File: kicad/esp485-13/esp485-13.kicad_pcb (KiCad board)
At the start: 2 copper layers, 22.2 x 20.3 mm, 16 parts, among them J1 Conn_01x08, U1 MAX3485, U2 ESP-WROOM-02, U3 AMS1117-3.3

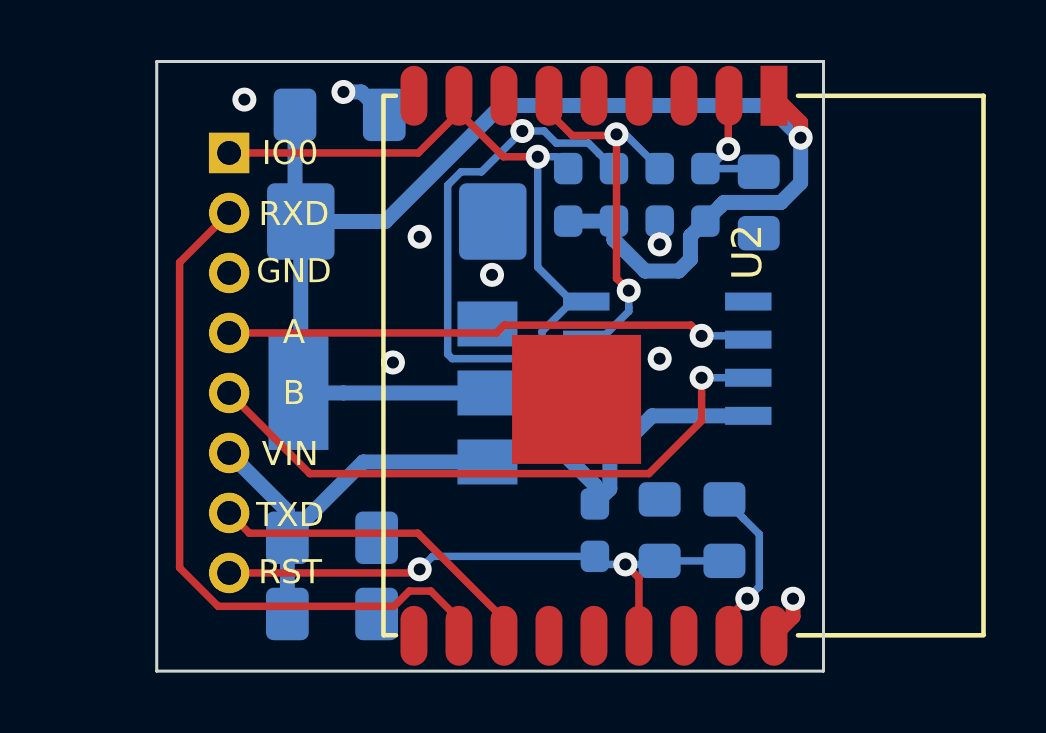
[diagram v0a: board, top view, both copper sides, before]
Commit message: arrange silks
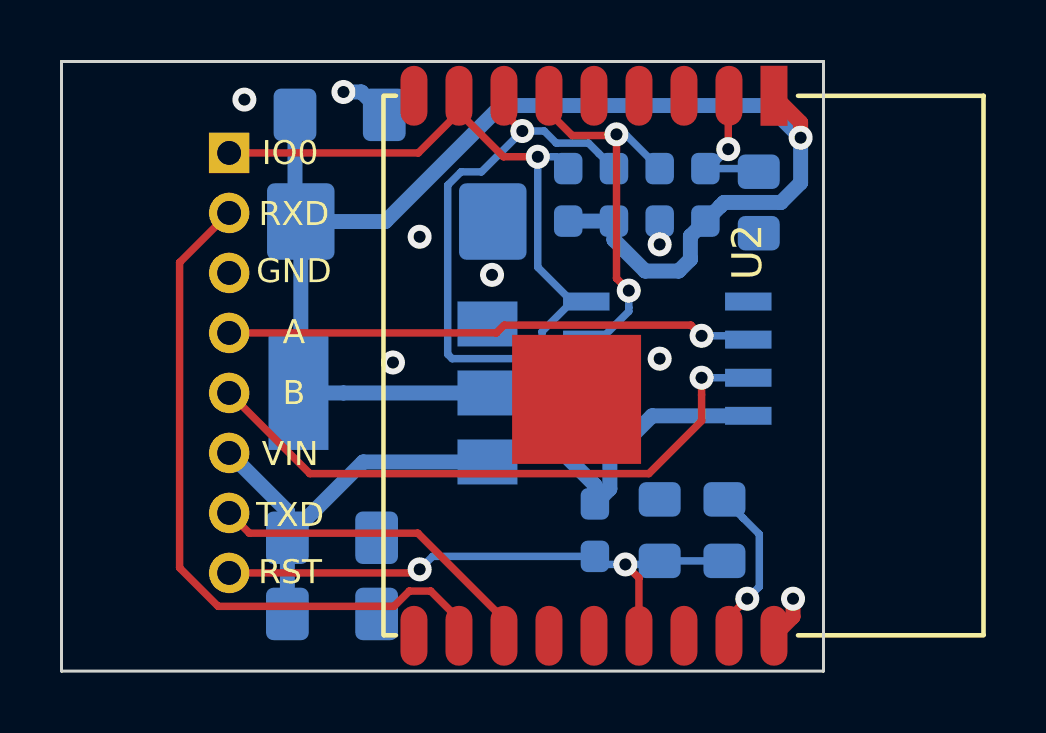
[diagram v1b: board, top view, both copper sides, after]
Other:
- board size 22.2 x 20.3 mm -> 25.4 x 20.3 mm
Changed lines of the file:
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@@
     (tags "capacitor handsolder")
     (attr smd)
-    (fp_text reference C1 (at -1.651 -1.778) (layer B.SilkS)
+    (fp_text reference C1 (at 3.683 0) (layer B.SilkS)
       (effects (font (size 1 1) (thickness 0.15)) (justify mirror))
     )
@@
     (tags "capacitor handsolder")
     (attr smd)
-    (fp_text reference C2 (at -3.175 1.143) (layer B.SilkS)
+    (fp_text reference C2 (at 3.683 0) (layer B.SilkS)
       (effects (font (size 1 1) (thickness 0.15)) (justify mirror))
     )
@@
     (tags "capacitor handsolder")
     (attr smd)
-    (fp_text reference C5 (at 2.667 0.042332 270) (layer B.SilkS)
+    (fp_text reference C5 (at -2.794 0.042332 270) (layer B.SilkS)
       (effects (font (size 1 1) (thickness 0.15)) (justify mirror))
     )
@@
     (tags "capacitor tantalum")
     (attr smd)
-    (fp_text reference C3 (at 0 0) (layer B.SilkS)
+    (fp_text reference C3 (at 0 -0.889) (layer B.SilkS)
       (effects (font (size 1 1) (thickness 0.15)) (justify mirror))
     )
@@
     (tags "capacitor handsolder")
     (attr smd)
-    (fp_text reference C6 (at 2.667 0 90) (layer B.SilkS)
+    (fp_text reference C6 (at -2.794 0 90) (layer B.SilkS)
       (effects (font (size 1 1) (thickness 0.15)) (justify mirror))
     )
@@
     (tags "resistor handsolder")
     (attr smd)
-    (fp_text reference R1 (at 2.413 0 270) (layer B.SilkS)
+    (fp_text reference R1 (at -2.54 0 270) (layer B.SilkS)
       (effects (font (size 1 1) (thickness 0.15)) (justify mirror))
     )
@@
     (tags "resistor handsolder")
     (attr smd)
-    (fp_text reference R2 (at 2.413 -0.254 270) (layer B.SilkS)
+    (fp_text reference R2 (at -2.54 0.635 270) (layer B.SilkS)
       (effects (font (size 1 1) (thickness 0.15)) (justify mirror))
     )
@@
     (tags "resistor handsolder")
     (attr smd)
-    (fp_text reference R3 (at 2.413 -0.127 90) (layer B.SilkS)
+    (fp_text reference R3 (at -2.794 0 90) (layer B.SilkS)
       (effects (font (size 1 1) (thickness 0.15)) (justify mirror))
     )
@@
     (tags "resistor handsolder")
     (attr smd)
-    (fp_text reference R7 (at -2.413 0.254 270) (layer B.SilkS)
+    (fp_text reference R7 (at -2.54 0.381 270) (layer B.SilkS)
       (effects (font (size 1 1) (thickness 0.15)) (justify mirror))
     )
@@
     (tags "resistor handsolder")
     (attr smd)
-    (fp_text reference R9 (at -2.286 -0.127 90) (layer B.SilkS)
+    (fp_text reference R9 (at 2.54 -0.127 90) (layer B.SilkS)
       (effects (font (size 1 1) (thickness 0.15)) (justify mirror))
     )
@@
     (descr "Through hole straight pin header, 1x08, 2.00mm pitch, single row")
     (tags "Through hole pin header THT 1x08 2.00mm single row")
-    (fp_text reference J1 (at 0 2.06 180) (layer B.SilkS)
+    (fp_text reference J1 (at 1.778 1.143 180) (layer B.SilkS)
       (effects (font (size 1 1) (thickness 0.15)) (justify mirror))
     )
@@
     (effects (font (size 1.5 1.5) (thickness 0.3)) (justify mirror))
   )
-  (dimension 28.575526 (width 0.3) (layer Cmts.User)
-    (gr_text "28.576 mm" (at 125.428164 133.608465 0.2546440579) (layer Cmts.User)
+  (dimension 31.115 (width 0.3) (layer Cmts.User)
+    (gr_text "31.115 mm" (at 124.1425 133.671999) (layer Cmts.User)
       (effects (font (size 1.5 1.5) (thickness 0.3)))
     )
-    (feature1 (pts (xy 139.700244 130.048) (xy 139.709059 132.031401)))
-    (feature2 (pts (xy 111.125 130.175) (xy 111.133815 132.158401)))
-    (crossbar (pts (xy 111.131209 131.571986) (xy 139.706453 131.444986)))
-    (arrow1a (pts (xy 139.706453 131.444986) (xy 138.582567 132.036408)))
-    (arrow1b (pts (xy 139.706453 131.444986) (xy 138.577354 130.863578)))
-    (arrow2a (pts (xy 111.131209 131.571986) (xy 112.260308 132.153394)))
-    (arrow2b (pts (xy 111.131209 131.571986) (xy 112.255095 130.980564)))
+    (feature1 (pts (xy 139.7 130.175) (xy 139.7 132.15842)))
+    (feature2 (pts (xy 108.585 130.175) (xy 108.585 132.15842)))
+    (crossbar (pts (xy 108.585 131.571999) (xy 139.7 131.571999)))
+    (arrow1a (pts (xy 139.7 131.571999) (xy 138.573496 132.15842)))
+    (arrow1b (pts (xy 139.7 131.571999) (xy 138.573496 130.985578)))
+    (arrow2a (pts (xy 108.585 131.571999) (xy 109.711504 132.15842)))
+    (arrow2b (pts (xy 108.585 131.571999) (xy 109.711504 130.985578)))
   )
   (gr_text + (at 114.681 112.014) (layer B.SilkS)
     (effects (font (size 1 1) (thickness 0.2)) (justify mirror))
   )
-  (gr_text + (at 114.935 109.22) (layer B.SilkS)
+  (gr_text + (at 115.57 108.585) (layer B.SilkS)
     (effects (font (size 1 1) (thickness 0.2)) (justify mirror))
   )
@@
     (arrow2b (pts (xy 143.816284 107.95) (xy 144.402705 109.076504)))
   )
-  (dimension 22.225 (width 0.3) (layer Cmts.User)
-    (gr_text "22.225 mm" (at 122.8725 103.31) (layer Cmts.User)
+  (dimension 25.4 (width 0.3) (layer Cmts.User)
+    (gr_text "25.400 mm" (at 121.285 103.31) (layer Cmts.User)
       (effects (font (size 1.5 1.5) (thickness 0.3)))
     )
-    (feature1 (pts (xy 111.76 106.68) (xy 111.76 104.823579)))
+    (feature1 (pts (xy 108.585 106.68) (xy 108.585 104.823579)))
     (feature2 (pts (xy 133.985 106.68) (xy 133.985 104.823579)))
-    (crossbar (pts (xy 133.985 105.41) (xy 111.76 105.41)))
-    (arrow1a (pts (xy 111.76 105.41) (xy 112.886504 104.823579)))
-    (arrow1b (pts (xy 111.76 105.41) (xy 112.886504 105.996421)))
+    (crossbar (pts (xy 133.985 105.41) (xy 108.585 105.41)))
+    (arrow1a (pts (xy 108.585 105.41) (xy 109.711504 104.823579)))
+    (arrow1b (pts (xy 108.585 105.41) (xy 109.711504 105.996421)))
     (arrow2a (pts (xy 133.985 105.41) (xy 132.858496 104.823579)))
     (arrow2b (pts (xy 133.985 105.41) (xy 132.858496 105.996421)))
   )
-  (gr_line (start 133.985 107.95) (end 111.76 107.95) (layer Edge.Cuts) (width 0.1))
-  (gr_line (start 111.76 128.27) (end 133.985 128.27) (layer Edge.Cuts) (width 0.1))
+  (gr_line (start 133.985 107.95) (end 108.585 107.95) (layer Edge.Cuts) (width 0.1))
+  (gr_line (start 108.585 128.27) (end 133.985 128.27) (layer Edge.Cuts) (width 0.1))
   (gr_line (start 133.985 128.27) (end 133.985 107.95) (layer Edge.Cuts) (width 0.1))
-  (gr_line (start 111.76 107.95) (end 111.76 128.27) (layer Edge.Cuts) (width 0.1))
+  (gr_line (start 108.585 107.95) (end 108.585 128.27) (layer Edge.Cuts) (width 0.1))
   (segment (start 116.1145 122.9395) (end 116.1145 123.825) (width 0.5) (layer B.Cu) (net 1))
   (segment (start 114.173 120.998) (end 116.1145 122.9395) (width 0.5) (layer B.Cu) (net 1))
@@
     (polygon
       (pts
-        (xy 111.76 107.95) (xy 133.985 107.95) (xy 133.985 128.27) (xy 111.76 128.27)
+        (xy 108.585 107.95) (xy 133.985 107.95) (xy 133.985 128.27) (xy 108.585 128.27)
       )
     )
@@
     (polygon
       (pts
-        (xy 111.76 107.95) (xy 133.985 107.95) (xy 133.985 128.27) (xy 111.76 128.27)
+        (xy 108.585 107.95) (xy 133.985 107.95) (xy 133.985 128.27) (xy 108.585 128.27)
       )
     )

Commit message: termination resistor added
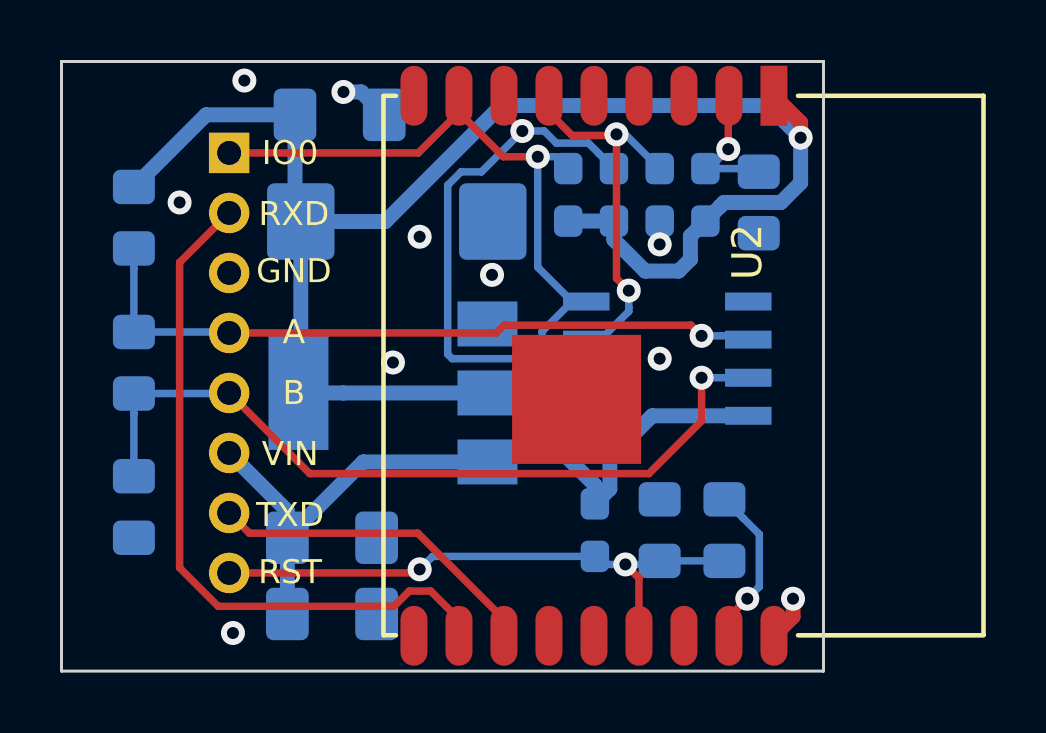
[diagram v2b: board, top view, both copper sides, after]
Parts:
- added R4: 1K, Resistor_SMD:R_0805_2012Metric_Pad1.15x1.40mm_HandSolder, B.Cu at (111.0, 122.8)
- added R5: 1K, Resistor_SMD:R_0805_2012Metric_Pad1.15x1.40mm_HandSolder, B.Cu at (111.0, 113.2)
- added R8: 120, Resistor_SMD:R_0805_2012Metric_Pad1.15x1.40mm_HandSolder, B.Cu at (111.0, 118.0)
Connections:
- U2 pad 10: (no net) -> Net-(U2-Pad10)
- U2 pad 14: (no net) -> Net-(U2-Pad14)
- U2 pad 16: (no net) -> Net-(U2-Pad16)
- U2 pad 3: (no net) -> Net-(U2-Pad3)
- U2 pad 4: (no net) -> Net-(U2-Pad4)
- U2 pad 5: (no net) -> Net-(U2-Pad5)
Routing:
- net +3V3: track 60.5 -> 66.9 mm
- net A: track 17.6 -> 23.6 mm
- net B: track 20.6 -> 26.5 mm
- net GND: vias 8 -> 10
